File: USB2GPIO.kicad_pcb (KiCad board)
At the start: 2 copper layers, 41.5 x 35 mm, 46 parts, among them J1 Conn_01x04, J7 Conn_01x03, J8 Conn_01x03, J9 Conn_01x02, Q1 S8050, Q10 Q_PNP_BEC, U10 PCA9554D, U11 HX9193, U12 SL2.1S, U2 CH340E, U3 CH340E, U9 ATtiny85V-10S, Y2 12M

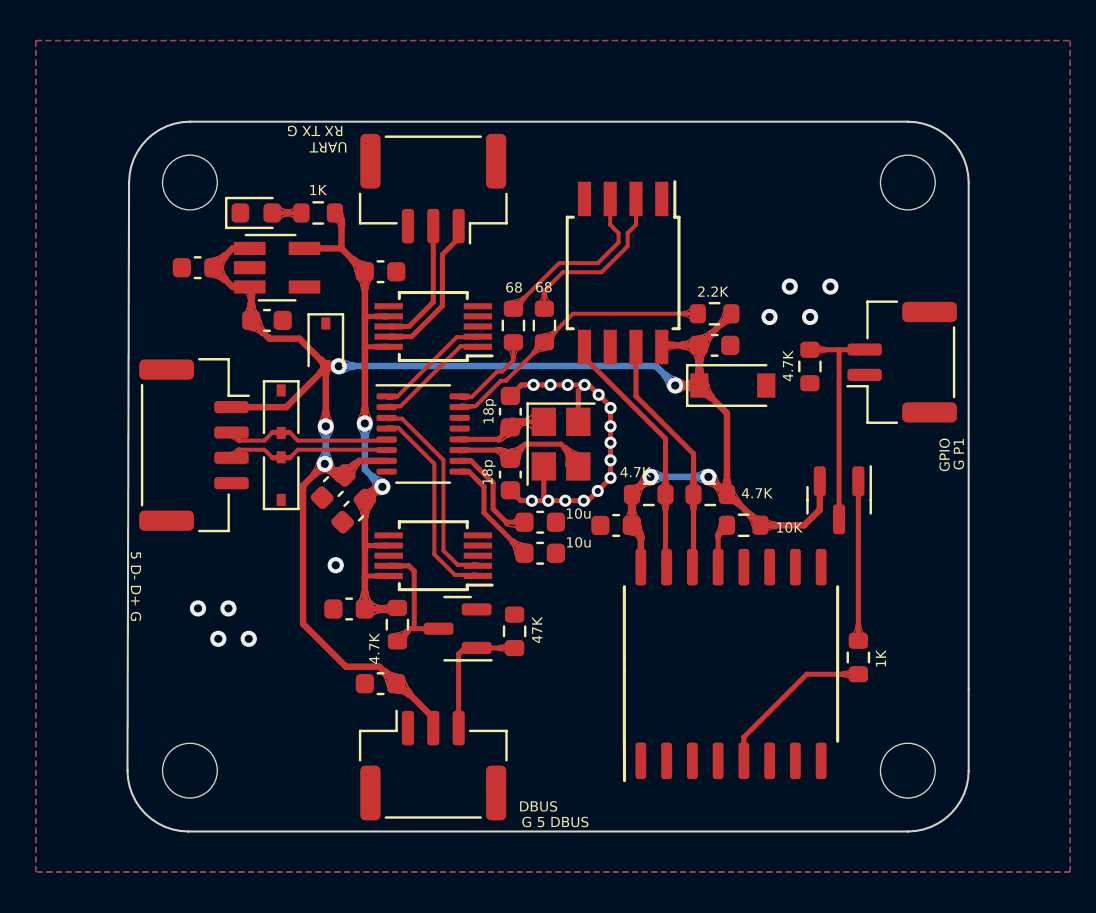
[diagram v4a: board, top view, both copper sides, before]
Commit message: Add output protect
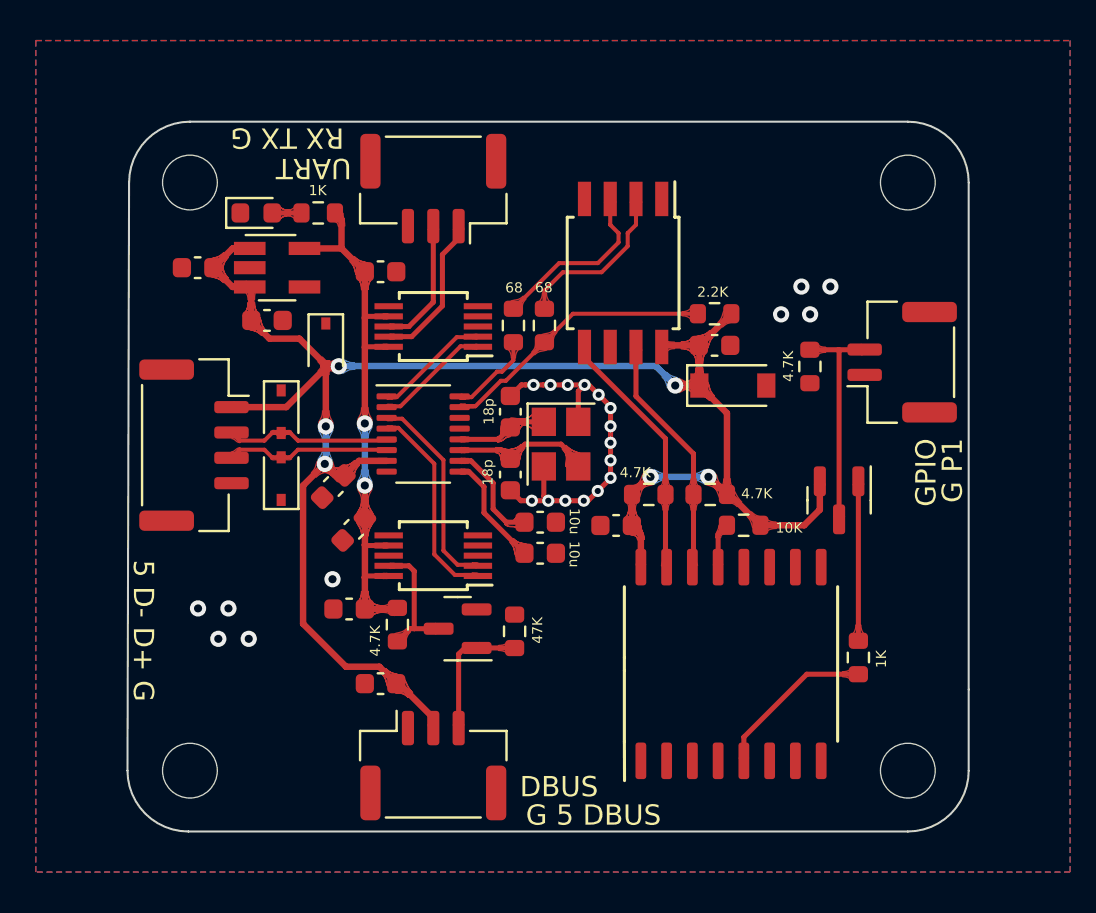
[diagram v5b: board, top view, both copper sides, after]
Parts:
- moved C7 0.90 mm to (48.7, 71.1)
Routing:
- net /3V3: track 29.2 -> 28.3 mm

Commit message: A try to add pull-up resistor for gpio_out
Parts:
- removed Q10: Q_PNP_BEC, Package_TO_SOT_SMD:SOT-23
- removed R31: 4.7K, Resistor_SMD:R_0603_1608Metric
- U10: value PCA9554D -> PCF8574T
- moved R30 6.70 mm to (72.0, 70.9), turned to 0 degrees
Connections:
- R30 pad 1: Net-(Q10-Pad1) -> +5V
- R30 pad 2: Net-(R30-Pad2) -> /GPIO/P1
- U10 pad 5: Net-(R30-Pad2) -> /GPIO/P1
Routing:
- net /GPIO/P1: track 11.1 -> 23.2 mm
- net Net-(R30-Pad2): track 8.10 -> 0.00 mm
- net Net-(Q10-Pad1): track 7.86 -> 0.00 mm
- net +5V: track 89.1 -> 86.9 mm
